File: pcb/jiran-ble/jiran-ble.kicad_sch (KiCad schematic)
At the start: 167 parts, among them J1 BATT, J2 USB-C Connector, J3 SWD, J4 BATT, J5 USB-C Connector, J6 SWD, Q1 SI2301CDS-T1-GE3, Q2 SI2301CDS-T1-GE3, SW10 SW_Push, SW11 SW_Push, SW12 SW_Push, SW13 SW_Push, SW14 SW_Push, SW15 SW_Push, SW16 SW_Push, SW17 SW_Push, SW18 SW_Push, SW19 SW_Push, SW2 SW_DPDT_x2, SW20 SW_Push, SW21 SW_Push, SW22 SW_Push, SW23 SW_Push, SW24 SW_Push, SW25 SW_Push, SW26 SW_Push, SW27 SW_Push, SW28 SW_Push, SW29 SW_Push, SW3 SW_Push, SW30 SW_Push, SW32 SW_Push, SW33 SW_Push, SW34 SW_Push, SW35 SW_Push, SW36 SW_Push, SW37 SW_Push, SW38 SW_Push, SW39 SW_Push, SW4 SW_Push, SW40 SW_Push, SW41 SW_Push, SW42 SW_Push, SW43 SW_Push, SW44 SW_Push, SW45 SW_Push, SW46 SW_Push, SW47 SW_Push, SW48 SW_Push, SW49 SW_Push, SW5 SW_Push, SW50 SW_Push, SW51 SW_Push, SW52 SW_Push, SW53 SW_Push, SW54 SW_Push, SW55 SW_Push, SW56 SW_Push, SW57 SW_Push, SW58 SW_Push, SW59 SW_Push, SW6 SW_Push, SW7 SW_Push, SW8 SW_Push, SW9 SW_Push, U1 HOLYIOT-18010-NRF52840_simple, U2 XC6220B331MR-G, U3 TP4054, U4 HOLYIOT-18010-NRF52840_simple, U5 XC6220B331MR-G, U6 TP4054

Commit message: Some graphic fixes
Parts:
- gave numbers to parts that had none: 2
- renumbered D31 to D30, D32 to D31, D33 to D32, D34 to D33, D35 to D34, D36 to D35, D37 to D36, D38 to D37, D39 to D38, D40 to D39, D41 to D40, D42 to D41, D43 to D42, D44 to D43, D45 to D44, D46 to D45, D47 to D46, D48 to D47, D49 to D48, D50 to D49, D51 to D50, D52 to D51, D53 to D52, D54 to D53, D55 to D54, D56 to D55, D57 to D56, D58 to D57, D30 to D58, J2 to J3, J3 to J4, J4 to J5, J5 to J7, J6 to J8, SW2 to SW1, SW11 to SW10, SW12 to SW11, SW13 to SW12, SW14 to SW13, SW15 to SW14, SW16 to SW15, SW17 to SW16, SW18 to SW17, SW19 to SW18, SW20 to SW19, SW3 to SW2, SW21 to SW20, SW22 to SW21, SW23 to SW22, SW24 to SW23, SW25 to SW24, SW26 to SW25, SW27 to SW26, SW28 to SW27, SW29 to SW28, SW30 to SW29, SW4 to SW3, SW32 to SW30, SW33 to SW31, SW34 to SW32, SW35 to SW33, SW36 to SW34, SW37 to SW35, SW38 to SW36, SW39 to SW37, SW40 to SW38, SW41 to SW39, SW5 to SW4, SW42 to SW40, SW43 to SW41, SW44 to SW42, SW45 to SW43, SW46 to SW44, SW47 to SW45, SW48 to SW46, SW49 to SW47, SW50 to SW48, SW51 to SW49, SW6 to SW5, SW52 to SW50, SW53 to SW51, SW54 to SW52, SW55 to SW53, SW56 to SW54, SW57 to SW55, SW58 to SW56, SW59 to SW57, SW7 to SW6, SW8 to SW7, SW9 to SW8, SW10 to SW9
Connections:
- net RESET_l: no longer J6.2 (Pin_2)
- net RESET_r: now also J6.2 (Pin_2)
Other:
- note added: "Left side contain: SW1 - SW30 D1 - D29 R1 - R9 HM1 - HM5 U1 - U3 J1 - J4 LED1 - LED2 C1 - C2 SW2A G1"
- note added: "Right side contain: SW31 - SW59 D30 - D58 R10 - R18 HM6 - HM10 U4 - U6 J5 - J8 LED3 - LED4 C3 - C4 SW2B G2"
- note removed: "Left side contain: SW1 - SW30 D1 - D29 R1 - R9 HM1 - HM5 U1 - U3 J1 - J3 LED1 - LED2 C1 - C2 SW2A G1"
- note removed: "Right side contain: SW31 - SW59 D30 - D58 R10 - R18 HM6 - HM10 U4 - U6 J4 - J6 LED3 - LED4 C3 - C4 SW2B G2"

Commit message: Change resistors nominal
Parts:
- C1, C2, C3, C4: footprint jiran-ble:Capacitor_SMD_0402 -> jiran-ble:C_0402
- D1, D10, D11, D12, D13, D14, D15, D16, D17, D18, D19, D2, D20, D21, D22, D23, D24, D25, D26, D27, D28, D29, D3, D30, D31, D32, D33, D34, D35, D36, D37, D38, D39, D4, D40, D41, D42, D43, D44, D45, D46, D47, D48, D49, D5, D50, D51, D52, D53, D54, D55, D56, D57, D58, D6, D7, D8, D9: footprint jiran-ble:Diode_SMD_SOD-123 -> jiran-ble:D_SOD-123
- J2, J6: footprint (none) -> jiran-ble:Connector_THT_1x2_2.54
- LED1, LED2, LED3, LED4: footprint jiran-ble:LED_SMD_0402 -> jiran-ble:LED_0603
- Q1, Q2: footprint jiran-ble:Package_SMD_SOT-23 -> jiran-ble:SOT-23
- R1, R2, R4, R5, R6, R7: footprint jiran-ble:Resistor_SMD_0402 -> jiran-ble:R_0402
- R11: value 820K -> 750K
- R3: value 820K -> 750K; footprint jiran-ble:Resistor_SMD_0402 -> jiran-ble:R_0402
- SW1: footprint (none) -> jiran-ble:Switch_SMD_MSK-12C02

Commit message: Assign footprints
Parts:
- R10, R12, R14, R15, R16, R8, R9: footprint jiran-ble:Resistor_SMD_0402 -> jiran-ble:R_0402
- R11, R13: footprint jiran-ble:Resistor_SMD_0402 -> jiran-ble:R_0603
- R3, R6: footprint jiran-ble:R_0402 -> jiran-ble:R_0603
- U2, U3, U5, U6: footprint jiran-ble:Package_SMD_SOT-23-5 -> jiran-ble:SOT-23-5
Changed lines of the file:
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@@
     (property "Reference" "R15" (id 0) (at 40.64 274.32 90))
     (property "Value" "1k" (id 1) (at 40.64 272.415 90))
-    (property "Footprint" "jiran-ble:Resistor_SMD_0402" (id 2) (at 40.64 268.732 90)
+    (property "Footprint" "jiran-ble:R_0402" (id 2) (at 40.64 268.732 90)
       (effects (font (size 1.27 1.27)) hide)
     )
@@
     (property "Reference" "R8" (id 0) (at 68.58 118.5672 90))
     (property "Value" "10k" (id 1) (at 68.58 120.8786 90))
-    (property "Footprint" "jiran-ble:Resistor_SMD_0402" (id 2) (at 68.58 122.047 90)
+    (property "Footprint" "jiran-ble:R_0402" (id 2) (at 68.58 122.047 90)
       (effects (font (size 1.27 1.27)) hide)
     )
@@
     (property "Reference" "R16" (id 0) (at 68.58 265.2522 90))
     (property "Value" "10k" (id 1) (at 68.58 267.5636 90))
-    (property "Footprint" "jiran-ble:Resistor_SMD_0402" (id 2) (at 68.58 268.732 90)
+    (property "Footprint" "jiran-ble:R_0402" (id 2) (at 68.58 268.732 90)
       (effects (font (size 1.27 1.27)) hide)
     )
@@
     (property "Reference" "R9" (id 0) (at 148.59 173.99 90))
     (property "Value" "5.1k" (id 1) (at 148.59 176.53 90))
-    (property "Footprint" "jiran-ble:Resistor_SMD_0402" (id 2) (at 148.59 178.435 0)
+    (property "Footprint" "jiran-ble:R_0402" (id 2) (at 148.59 178.435 0)
       (effects (font (size 1.27 1.27)) hide)
     )
@@
     (property "Reference" "R10" (id 0) (at 148.59 185.42 90))
     (property "Value" "5.1k" (id 1) (at 148.59 182.88 90))
-    (property "Footprint" "jiran-ble:Resistor_SMD_0402" (id 2) (at 148.59 180.975 0)
+    (property "Footprint" "jiran-ble:R_0402" (id 2) (at 148.59 180.975 0)
       (effects (font (size 1.27 1.27)) hide)
     )
@@
     (property "Reference" "R14" (id 0) (at 201.295 202.0316 90))
     (property "Value" "1k" (id 1) (at 201.295 204.343 90))
-    (property "Footprint" "jiran-ble:Resistor_SMD_0402" (id 2) (at 201.295 207.01 0)
+    (property "Footprint" "jiran-ble:R_0402" (id 2) (at 201.295 207.01 0)
       (effects (font (size 1.27 1.27)) hide)
     )
@@
       (effects (font (size 1.27 1.27)) (justify left))
     )
-    (property "Footprint" "jiran-ble:Resistor_SMD_0402" (id 2) (at 307.848 203.835 90)
+    (property "Footprint" "jiran-ble:R_0402" (id 2) (at 307.848 203.835 90)
       (effects (font (size 1.27 1.27)) hide)
     )
@@
       (effects (font (size 1.27 1.27)) (justify left))
     )
-    (property "Footprint" "jiran-ble:R_0402" (id 2) (at 389.382 59.055 90)
+    (property "Footprint" "jiran-ble:R_0603" (id 2) (at 389.382 59.055 90)
       (effects (font (size 1.27 1.27)) hide)
     )
@@
       (effects (font (size 1.27 1.27)) (justify left))
     )
-    (property "Footprint" "jiran-ble:R_0402" (id 2) (at 389.382 69.85 90)
+    (property "Footprint" "jiran-ble:R_0603" (id 2) (at 389.382 69.85 90)
       (effects (font (size 1.27 1.27)) hide)
     )
@@
       (effects (font (size 1.27 1.27)) (justify left))
     )
-    (property "Footprint" "jiran-ble:Resistor_SMD_0402" (id 2) (at 390.017 193.675 90)
+    (property "Footprint" "jiran-ble:R_0603" (id 2) (at 390.017 193.675 90)
       (effects (font (size 1.27 1.27)) hide)
     )
@@
       (effects (font (size 1.27 1.27)) (justify left))
     )
-    (property "Footprint" "jiran-ble:Resistor_SMD_0402" (id 2) (at 390.017 204.47 90)
+    (property "Footprint" "jiran-ble:R_0603" (id 2) (at 390.017 204.47 90)
       (effects (font (size 1.27 1.27)) hide)
     )
@@
     (property "Reference" "U2" (id 0) (at 330.2 57.9882 0))
     (property "Value" "XC6220B331MR-G" (id 1) (at 330.2 60.2996 0))
-    (property "Footprint" "jiran-ble:Package_SMD_SOT-23-5" (id 2) (at 330.2 58.42 0)
+    (property "Footprint" "jiran-ble:SOT-23-5" (id 2) (at 330.2 58.42 0)
       (effects (font (size 1.27 1.27)) hide)
     )
@@
     (property "Reference" "U5" (id 0) (at 330.835 192.6082 0))
     (property "Value" "XC6220B331MR-G" (id 1) (at 330.835 194.9196 0))
-    (property "Footprint" "jiran-ble:Package_SMD_SOT-23-5" (id 2) (at 330.835 193.04 0)
+    (property "Footprint" "jiran-ble:SOT-23-5" (id 2) (at 330.835 193.04 0)
       (effects (font (size 1.27 1.27)) hide)
     )
@@
     (property "Reference" "U3" (id 0) (at 59.055 112.395 0))
     (property "Value" "TP4054" (id 1) (at 59.055 114.935 0))
-    (property "Footprint" "jiran-ble:Package_SMD_SOT-23-5" (id 2) (at 53.34 127.635 0)
+    (property "Footprint" "jiran-ble:SOT-23-5" (id 2) (at 53.34 127.635 0)
       (effects (font (size 1.27 1.27) italic) (justify left) hide)
     )
@@
     (property "Reference" "U6" (id 0) (at 59.055 259.08 0))
     (property "Value" "TP4054" (id 1) (at 59.055 261.62 0))
-    (property "Footprint" "jiran-ble:Package_SMD_SOT-23-5" (id 2) (at 53.34 274.32 0)
+    (property "Footprint" "jiran-ble:SOT-23-5" (id 2) (at 53.34 274.32 0)
       (effects (font (size 1.27 1.27) italic) (justify left) hide)
     )
@@
     )
     (path "/00000000-0000-0000-0000-00005ed6d985"
-      (reference "R3") (unit 1) (value "750K") (footprint "jiran-ble:R_0402")
+      (reference "R3") (unit 1) (value "750K") (footprint "jiran-ble:R_0603")
     )
     (path "/00000000-0000-0000-0000-000060dd5462"
@@
     )
     (path "/00000000-0000-0000-0000-00005ed6ea28"
-      (reference "R6") (unit 1) (value "2M") (footprint "jiran-ble:R_0402")
+      (reference "R6") (unit 1) (value "2M") (footprint "jiran-ble:R_0603")
     )
     (path "/00000000-0000-0000-0000-00005f6fefa4"
@@
     )
     (path "/00000000-0000-0000-0000-00005ed0e40c"
-      (reference "R8") (unit 1) (value "10k") (footprint "jiran-ble:Resistor_SMD_0402")
+      (reference "R8") (unit 1) (value "10k") (footprint "jiran-ble:R_0402")
     )
     (path "/00000000-0000-0000-0000-00006130bf72"
-      (reference "R9") (unit 1) (value "5.1k") (footprint "jiran-ble:Resistor_SMD_0402")
+      (reference "R9") (unit 1) (value "5.1k") (footprint "jiran-ble:R_0402")
     )
     (path "/00000000-0000-0000-0000-00006130bf78"
-      (reference "R10") (unit 1) (value "5.1k") (footprint "jiran-ble:Resistor_SMD_0402")
+      (reference "R10") (unit 1) (value "5.1k") (footprint "jiran-ble:R_0402")
     )
     (path "/00000000-0000-0000-0000-00006130bd03"
-      (reference "R11") (unit 1) (value "750K") (footprint "jiran-ble:Resistor_SMD_0402")
+      (reference "R11") (unit 1) (value "750K") (footprint "jiran-ble:R_0603")
     )
     (path "/00000000-0000-0000-0000-00006130bcd5"
-      (reference "R12") (unit 1) (value "100K") (footprint "jiran-ble:Resistor_SMD_0402")
+      (reference "R12") (unit 1) (value "100K") (footprint "jiran-ble:R_0402")
     )
     (path "/00000000-0000-0000-0000-00006130bcfd"
-      (reference "R13") (unit 1) (value "2M") (footprint "jiran-ble:Resistor_SMD_0402")
+      (reference "R13") (unit 1) (value "2M") (footprint "jiran-ble:R_0603")
     )
     (path "/00000000-0000-0000-0000-00006130bfa8"
-      (reference "R14") (unit 1) (value "1k") (footprint "jiran-ble:Resistor_SMD_0402")
+      (reference "R14") (unit 1) (value "1k") (footprint "jiran-ble:R_0402")
     )
     (path "/00000000-0000-0000-0000-00006130bd32"
-      (reference "R15") (unit 1) (value "1k") (footprint "jiran-ble:Resistor_SMD_0402")
+      (reference "R15") (unit 1) (value "1k") (footprint "jiran-ble:R_0402")
     )
     (path "/00000000-0000-0000-0000-00006130bcf5"
-      (reference "R16") (unit 1) (value "10k") (footprint "jiran-ble:Resistor_SMD_0402")
+      (reference "R16") (unit 1) (value "10k") (footprint "jiran-ble:R_0402")
     )
     (path "/b96e24a5-8cbd-40bf-b134-58cd8137e945"
@@
     )
     (path "/00000000-0000-0000-0000-00005ebf7400"
-      (reference "U2") (unit 1) (value "XC6220B331MR-G") (footprint "jiran-ble:Package_SMD_SOT-23-5")
+      (reference "U2") (unit 1) (value "XC6220B331MR-G") (footprint "jiran-ble:SOT-23-5")
     )
     (path "/00000000-0000-0000-0000-00005ec2c51f"
-      (reference "U3") (unit 1) (value "TP4054") (footprint "jiran-ble:Package_SMD_SOT-23-5")
+      (reference "U3") (unit 1) (value "TP4054") (footprint "jiran-ble:SOT-23-5")
     )
     (path "/00000000-0000-0000-0000-00006130bf27"
@@
     )
     (path "/00000000-0000-0000-0000-00006130bce8"
-      (reference "U5") (unit 1) (value "XC6220B331MR-G") (footprint "jiran-ble:Package_SMD_SOT-23-5")
+      (reference "U5") (unit 1) (value "XC6220B331MR-G") (footprint "jiran-ble:SOT-23-5")
     )
     (path "/00000000-0000-0000-0000-00006130bcef"
-      (reference "U6") (unit 1) (value "TP4054") (footprint "jiran-ble:Package_SMD_SOT-23-5")
+      (reference "U6") (unit 1) (value "TP4054") (footprint "jiran-ble:SOT-23-5")
     )
   )

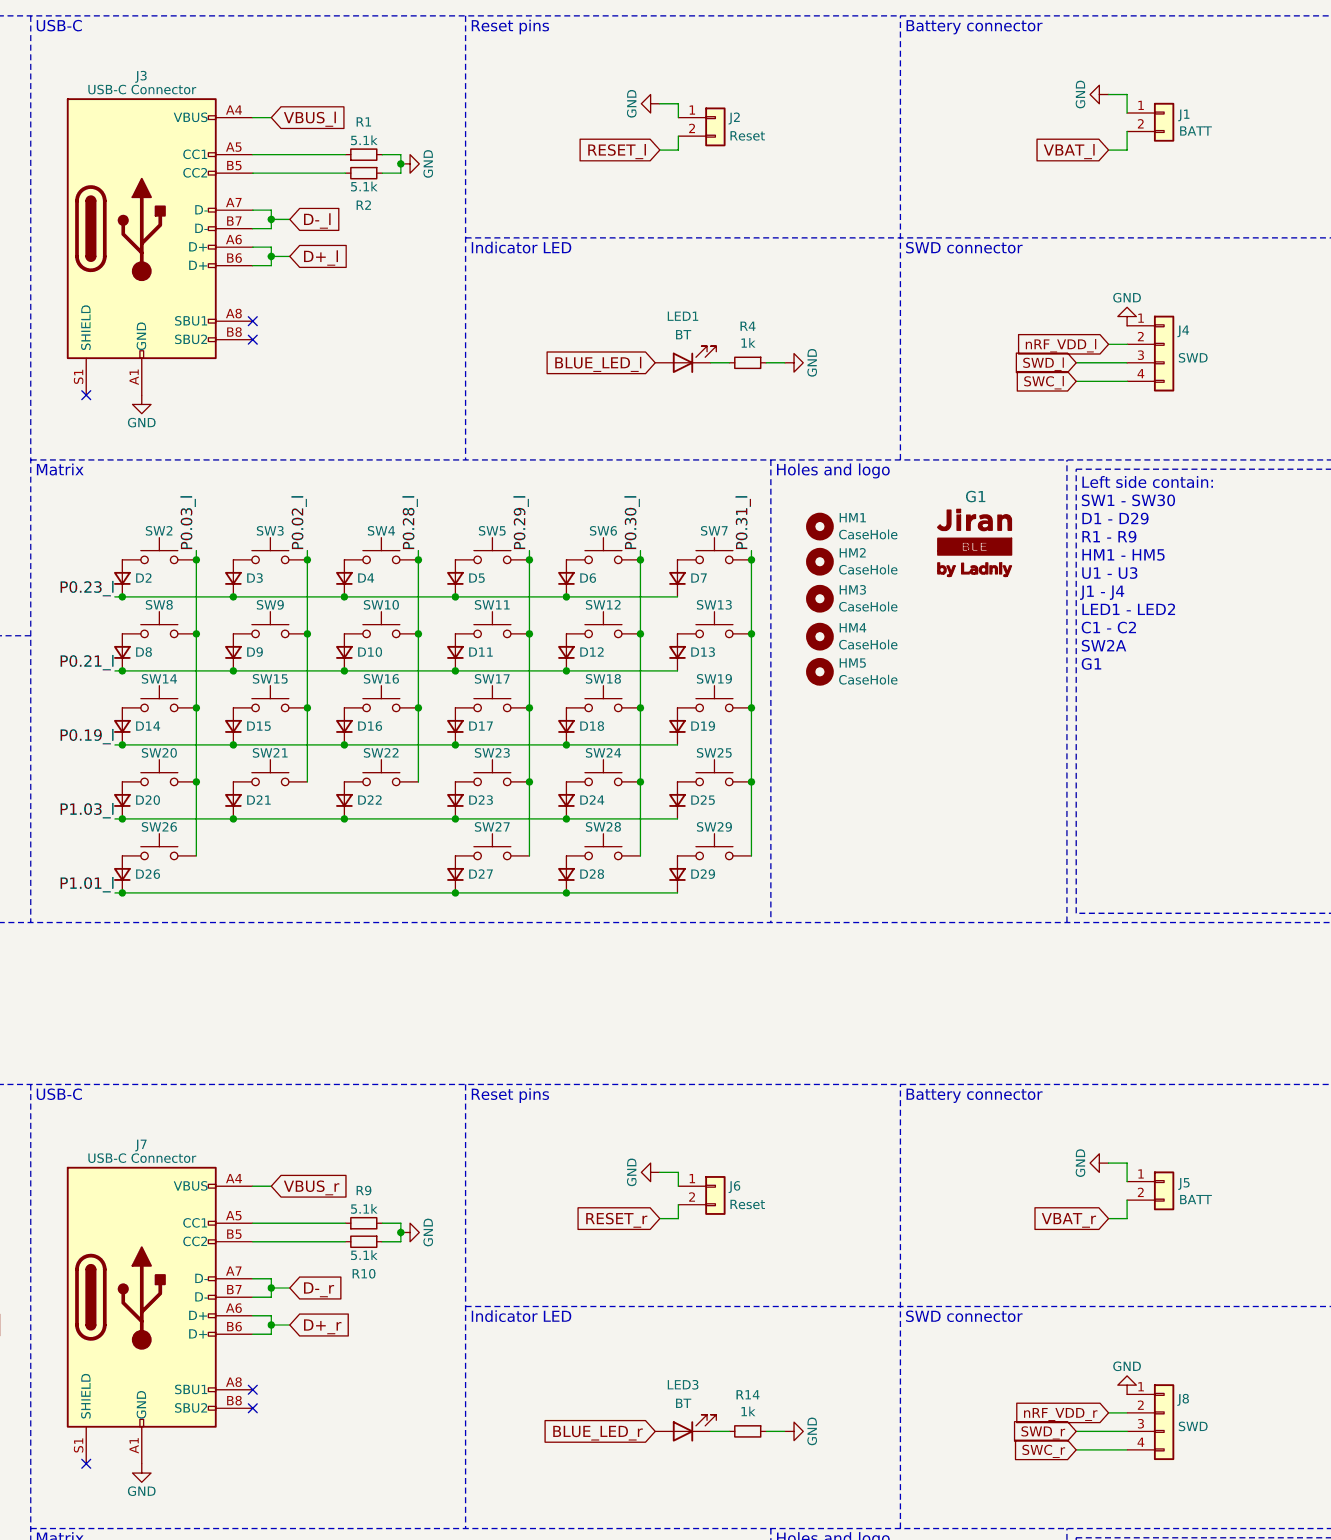
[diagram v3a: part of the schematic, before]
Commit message: Return reset button
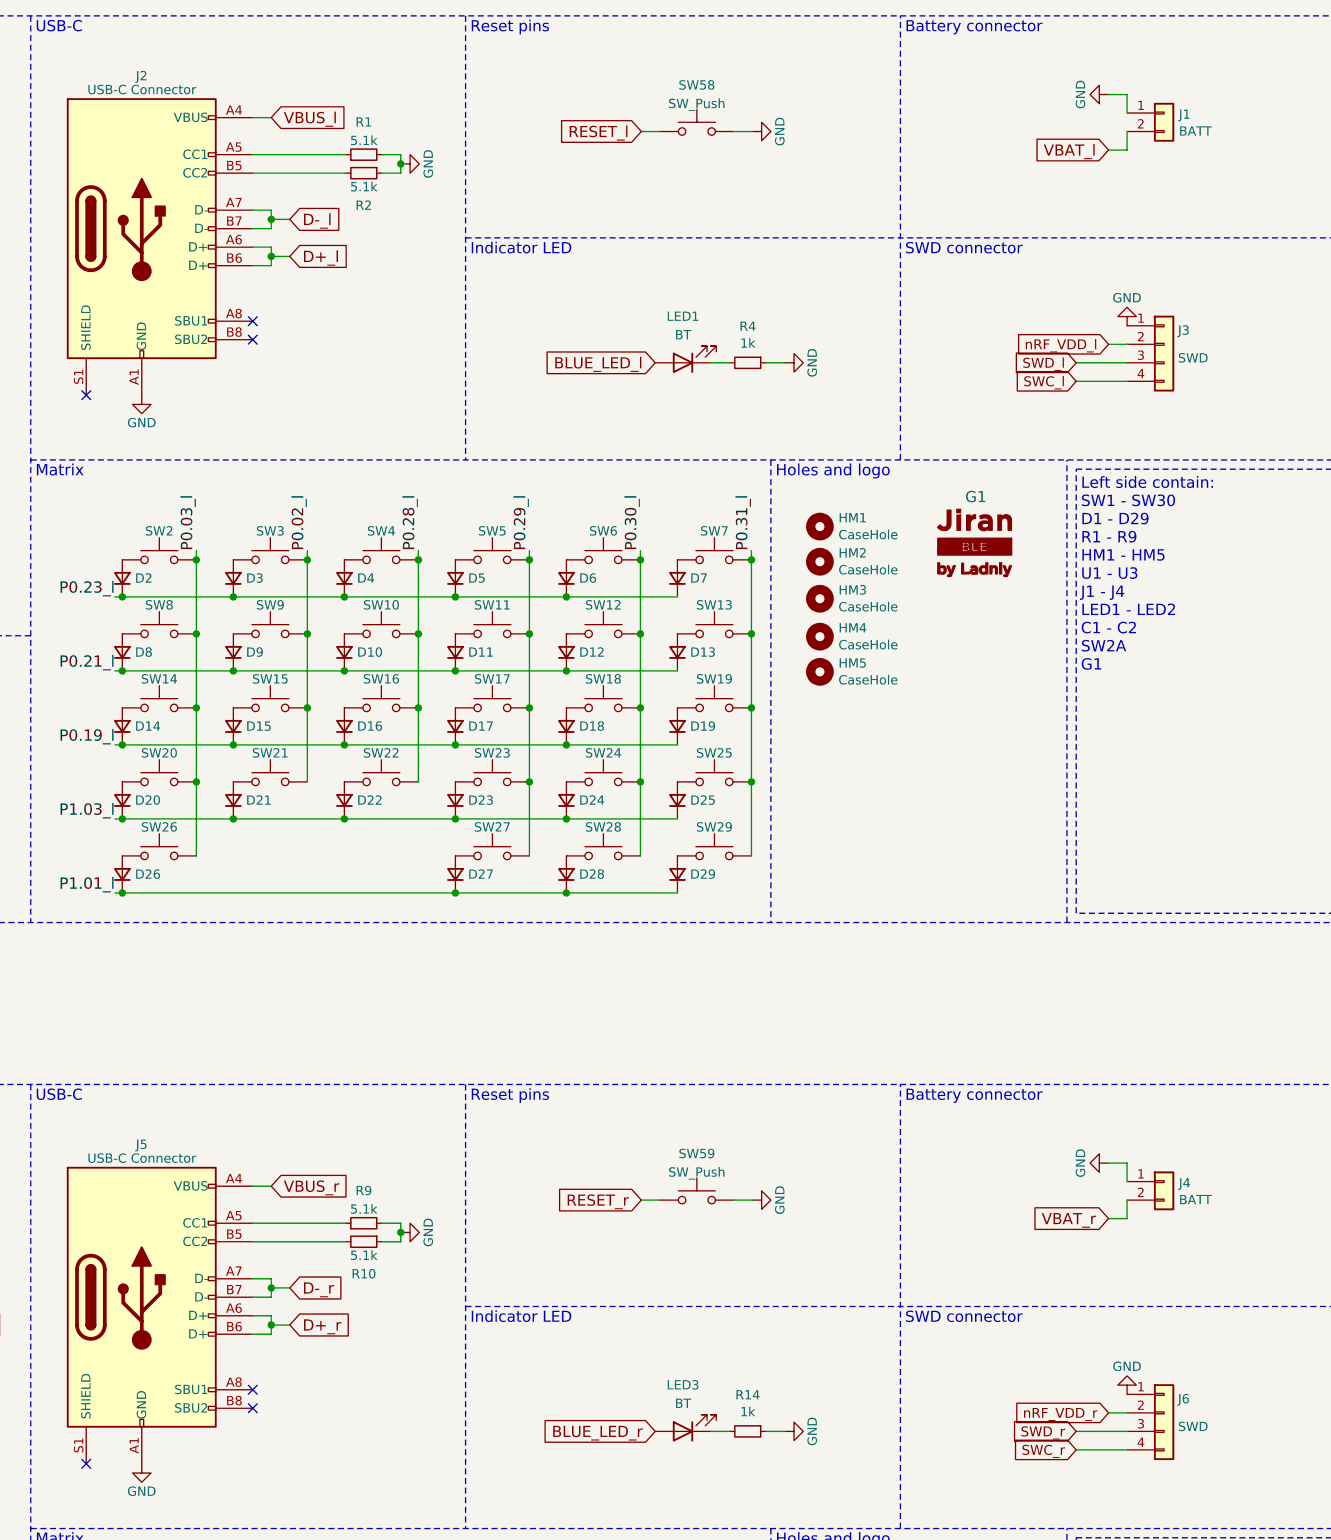
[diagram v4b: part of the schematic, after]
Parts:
- removed J2, J6: Reset, jiran-ble:Connector_THT_1x2_2.54, symbol Connector_Generic:Conn_01x02
- added SW58, SW59: SW_Push, symbol Switch:SW_Push
- renumbered J3 to J2, J4 to J3, J5 to J4, J7 to J5, J8 to J6
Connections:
- net GND: now also SW58.2, SW59.2
- net RESET_l: now also SW58.1
- net RESET_r: now also SW59.1
